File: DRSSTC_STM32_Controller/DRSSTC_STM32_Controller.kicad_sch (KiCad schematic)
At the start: 4 parts, among them J2 Conn_01x04

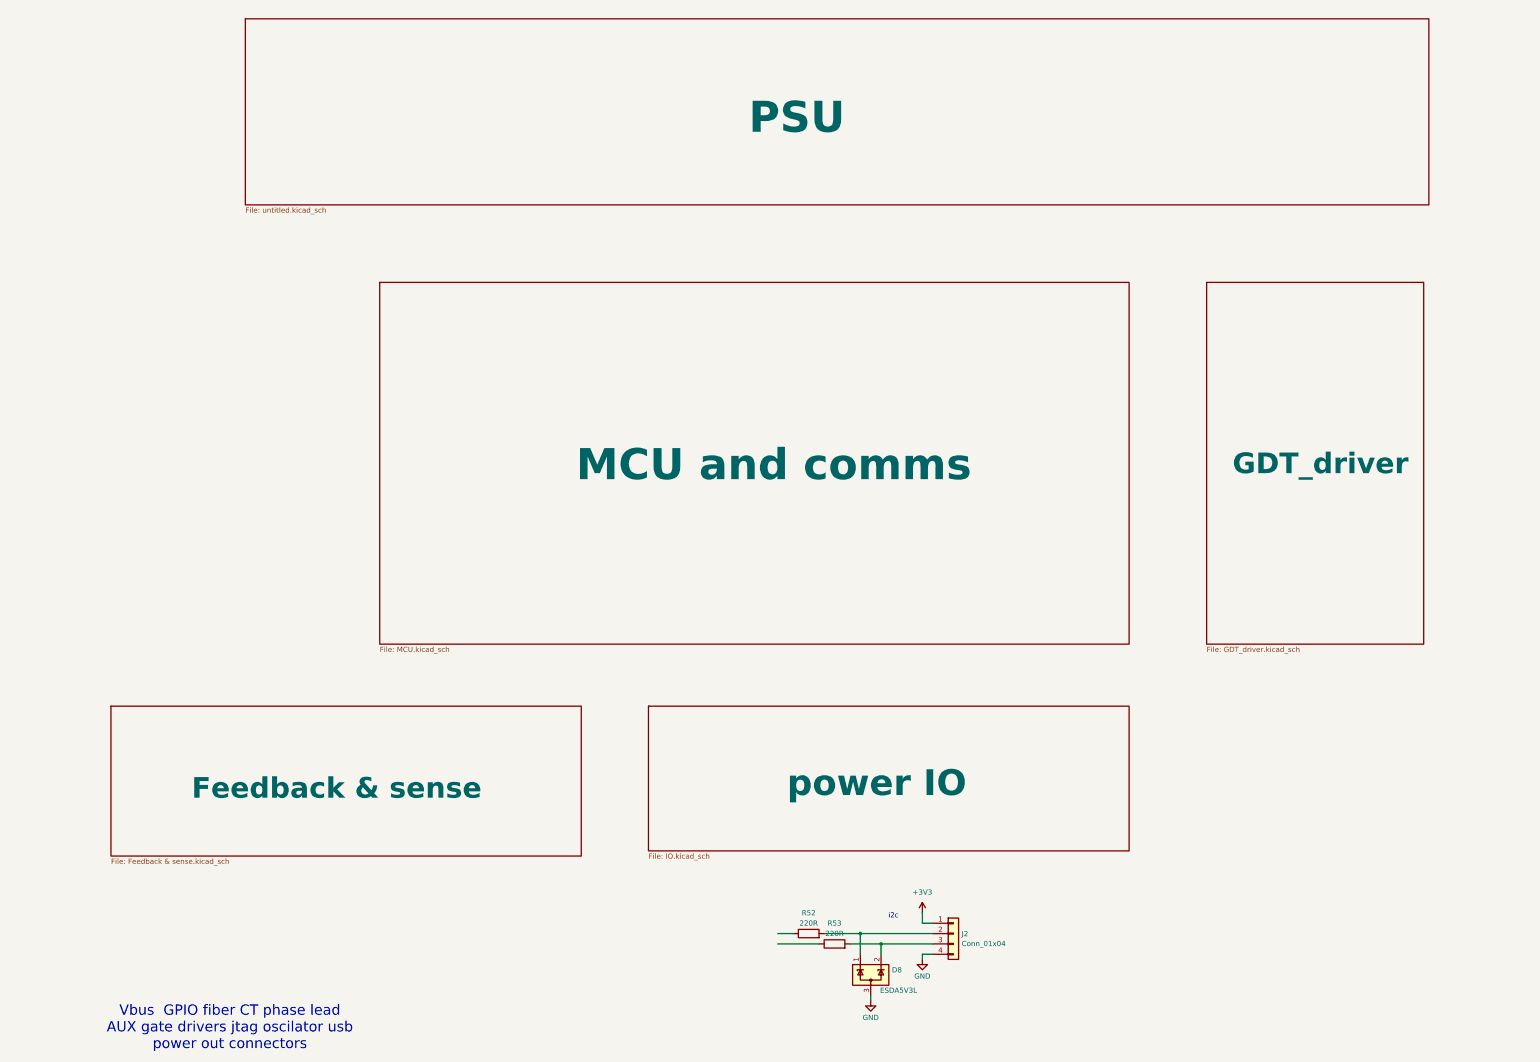
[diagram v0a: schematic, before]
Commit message: update the feedback stage simulation & controller schematic
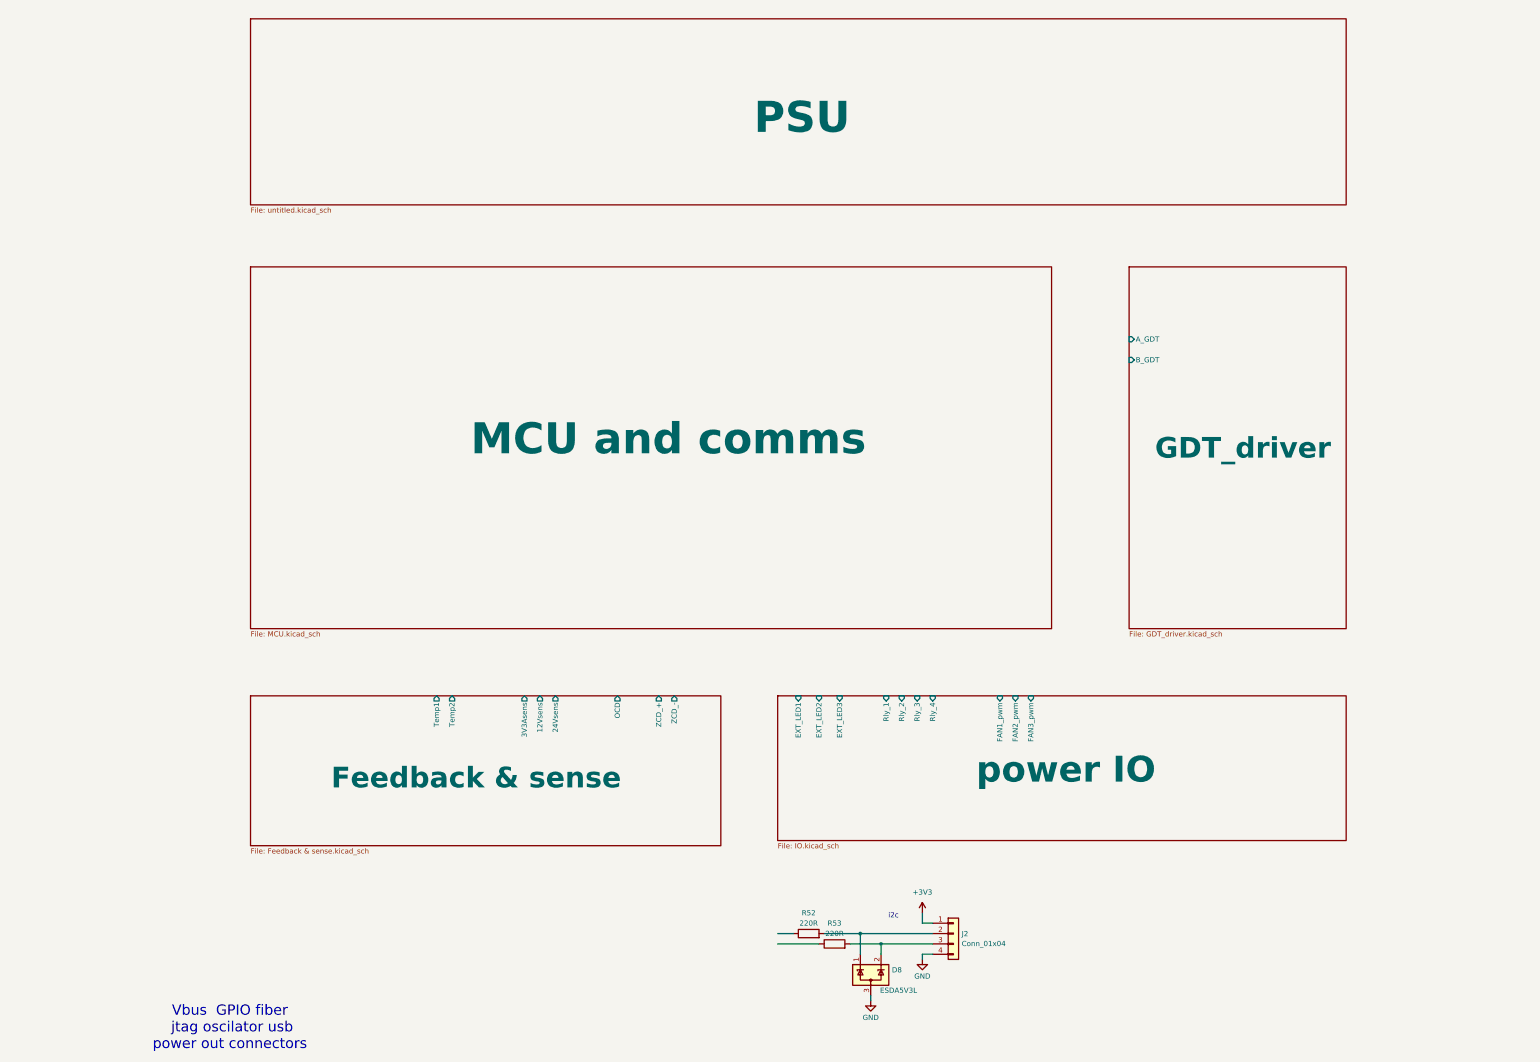
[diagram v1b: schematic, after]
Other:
- sheet Feedback & sense ports: added 12Vsens, 24Vsens, 3V3Asens, OCD, Temp1, Temp2, ZCD_+, ZCD_-; removed none
- sheet GDT_driver ports: added A_GDT, B_GDT; removed none
- sheet power IO ports: added EXT_LED1, EXT_LED2, EXT_LED3, FAN1_pwm, FAN2_pwm, FAN3_pwm, Rly_1, Rly_2, Rly_3, Rly_4; removed none
- note added: "Vbus GPIO fiber jtag oscilator usb power out connectors"
- note removed: "Vbus GPIO fiber CT phase lead AUX gate drivers jtag oscilator usb power out connectors"
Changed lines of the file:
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@@
 	(generator_version "10.0")
 	(paper "A3")
-	(text "Vbus  GPIO fiber CT phase lead\nAUX gate drivers jtag oscilator usb\npower out connectors"
+	(text "Vbus  GPIO fiber \n jtag oscilator usb\npower out connectors"
 		(exclude_from_sim no)
 		(at 72.39 270.764 0)
@@
 	)
 	(sheet
-		(at 312.42 87.63)
+		(at 293.37 83.82)
 		(size 53.34 88.9)
 		(exclude_from_sim no)
@@
 		)
 		(property "Sheetname" "GDT_driver"
-			(at 318.77 135.128 0)
+			(at 299.72 131.318 0)
 			(show_name no)
 			(do_not_autoplace no)
@@
 		)
 		(property "Sheetfile" "GDT_driver.kicad_sch"
-			(at 312.42 177.1146 0)
+			(at 293.37 173.3046 0)
 			(show_name no)
 			(do_not_autoplace no)
@@
 				)
 				(justify left top)
+			)
+		)
+		(pin "A_GDT" input
+			(at 293.37 101.6 180)
+			(effects
+				(font
+					(size 1.27 1.27)
+				)
+				(justify left)
+			)
+		)
+		(pin "B_GDT" input
+			(at 293.37 106.68 180)
+			(effects
+				(font
+					(size 1.27 1.27)
+				)
+				(justify left)
 			)
 		)
@@
 	)
 	(sheet
-		(at 109.22 87.63)
-		(size 184.15 88.9)
+		(at 77.47 83.82)
+		(size 196.85 88.9)
 		(exclude_from_sim no)
 		(in_bom yes)
@@
 		)
 		(property "Sheetname" "MCU and comms"
-			(at 157.48 136.906 0)
+			(at 131.572 130.556 0)
 			(show_name no)
 			(do_not_autoplace no)
@@
 		)
 		(property "Sheetfile" "MCU.kicad_sch"
-			(at 109.22 177.1146 0)
+			(at 77.47 173.3046 0)
 			(show_name no)
 			(do_not_autoplace no)
@@
 	)
 	(sheet
-		(at 76.2 22.86)
-		(size 290.83 45.72)
+		(at 77.47 22.86)
+		(size 269.24 45.72)
 		(exclude_from_sim no)
 		(in_bom yes)
@@
 		)
 		(property "Sheetname" "PSU"
-			(at 199.898 51.562 0)
+			(at 201.168 51.562 0)
 			(show_name no)
 			(do_not_autoplace no)
@@
 		)
 		(property "Sheetfile" "untitled.kicad_sch"
-			(at 76.2 69.1646 0)
+			(at 77.47 69.1646 0)
 			(show_name no)
 			(do_not_autoplace no)
@@
 	)
 	(sheet
-		(at 43.18 191.77)
+		(at 77.47 189.23)
 		(size 115.57 36.83)
 		(exclude_from_sim no)
@@
 		)
 		(property "Sheetname" "Feedback & sense"
-			(at 62.992 214.884 0)
+			(at 97.282 212.344 0)
 			(show_name no)
 			(do_not_autoplace no)
@@
 		)
 		(property "Sheetfile" "Feedback & sense.kicad_sch"
-			(at 43.18 229.1846 0)
+			(at 77.47 226.6446 0)
 			(show_name no)
 			(do_not_autoplace no)
@@
 				)
 				(justify left top)
+			)
+		)
+		(pin "3V3Asens" output
+			(at 144.78 189.23 90)
+			(effects
+				(font
+					(size 1.27 1.27)
+				)
+				(justify right)
+			)
+		)
+		(pin "12Vsens" output
+			(at 148.59 189.23 90)
+			(effects
+				(font
+					(size 1.27 1.27)
+				)
+				(justify right)
+			)
+		)
+		(pin "24Vsens" output
+			(at 152.4 189.23 90)
+			(effects
+				(font
+					(size 1.27 1.27)
+				)
+				(justify right)
+			)
+		)
+		(pin "OCD" output
+			(at 167.64 189.23 90)
+			(effects
+				(font
+					(size 1.27 1.27)
+				)
+				(justify right)
+			)
+		)
+		(pin "Temp1" output
+			(at 123.19 189.23 90)
+			(effects
+				(font
+					(size 1.27 1.27)
+				)
+				(justify right)
+			)
+		)
+		(pin "Temp2" output
+			(at 127 189.23 90)
+			(effects
+				(font
+					(size 1.27 1.27)
+				)
+				(justify right)
+			)
+		)
+		(pin "ZCD_+" output
+			(at 177.8 189.23 90)
+			(effects
+				(font
+					(size 1.27 1.27)
+				)
+				(justify right)
+			)
+		)
+		(pin "ZCD_-" output
+			(at 181.61 189.23 90)
+			(effects
+				(font
+					(size 1.27 1.27)
+				)
+				(justify right)
 			)
 		)
@@
 	)
 	(sheet
-		(at 175.26 191.77)
-		(size 118.11 35.56)
+		(at 207.01 189.23)
+		(size 139.7 35.56)
 		(exclude_from_sim no)
 		(in_bom yes)
@@
 		)
 		(property "Sheetname" "power IO"
-			(at 209.296 214.376 0)
+			(at 255.778 211.074 0)
 			(show_name no)
 			(do_not_autoplace no)
@@
 		)
 		(property "Sheetfile" "IO.kicad_sch"
-			(at 175.26 227.9146 0)
+			(at 207.01 225.3746 0)
 			(show_name no)
 			(do_not_autoplace no)
@@
 			)
 		)
+		(pin "EXT_LED1" input
+			(at 212.09 189.23 90)
+			(effects
+				(font
+					(size 1.27 1.27)
+				)
+				(justify right)
+			)
+		)
+		(pin "EXT_LED2" input
+			(at 217.17 189.23 90)
+			(effects
+				(font
+					(size 1.27 1.27)
+				)
+				(justify right)
+			)
+		)
+		(pin "EXT_LED3" input
+			(at 222.25 189.23 90)
+			(effects
+				(font
+					(size 1.27 1.27)
+				)
+				(justify right)
+			)
+		)
+		(pin "FAN1_pwm" input
+			(at 261.62 189.23 90)
+			(effects
+				(font
+					(size 1.27 1.27)
+				)
+				(justify right)
+			)
+		)
+		(pin "FAN2_pwm" input
+			(at 265.43 189.23 90)
+			(effects
+				(font
+					(size 1.27 1.27)
+				)
+				(justify right)
+			)
+		)
+		(pin "FAN3_pwm" input
+			(at 269.24 189.23 90)
+			(effects
+				(font
+					(size 1.27 1.27)
+				)
+				(justify right)
+			)
+		)
+		(pin "Rly_1" input
+			(at 233.68 189.23 90)
+			(effects
+				(font
+					(size 1.27 1.27)
+				)
+				(justify right)
+			)
+		)
+		(pin "Rly_2" input
+			(at 237.49 189.23 90)
+			(effects
+				(font
+					(size 1.27 1.27)
+				)
+				(justify right)
+			)
+		)
+		(pin "Rly_3" input
+			(at 241.3 189.23 90)
+			(effects
+				(font
+					(size 1.27 1.27)
+				)
+				(justify right)
+			)
+		)
+		(pin "Rly_4" input
+			(at 245.11 189.23 90)
+			(effects
+				(font
+					(size 1.27 1.27)
+				)
+				(justify right)
+			)
+		)

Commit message: update conroller schematics
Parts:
- removed D8: ESDA5V3L, Package_TO_SOT_SMD:SOT-23-3, symbol Power_Protection:ESDA5V3L
- removed J2: Conn_01x04, symbol Connector_Generic:Conn_01x04
- removed R52, R53: 220R, Resistor_SMD:R_0805_2012Metric, symbol Device:R
- added C48: 10n, Capacitor_SMD:C_0805_2012Metric, symbol Device:C
- added C49: 10u, Capacitor_SMD:C_0805_2012Metric, symbol Device:C
- added D42, D44: D_Schottky, symbol Device:D_Schottky
- added J1, J10, J11, J16, J7: Conn_01x04, symbol Connector_Generic:Conn_01x04
- added J13: USB_C_Receptacle_USB2.0_14P, symbol Connector:USB_C_Receptacle_USB2.0_14P
- added J28, J29, J30, J31, J32, J33, J34, J35, J36, J37, J38, J39, J4, J40, J41, J42: Screw_Terminal_01x02, TerminalBlock_Altech:Altech_AK100_1x02_P5.00mm, symbol Connector:Screw_Terminal_01x02
- added J5, J6: Conn_01x01, symbol Connector_Generic:Conn_01x01
- added JP4: SolderJumper_2_Bridged, symbol Jumper:SolderJumper_2_Bridged
- added R76: 1M, Resistor_SMD:R_0805_2012Metric, symbol Device:R
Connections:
- net +3V3: now also D44.1 (K)
- net GND: now also C48.2, C49.2, J1.1 (Pin_1), J10.1 (Pin_1), J11.1 (Pin_1), J13.A1 (GND), J13.A12 (GND), J13.B1 (GND), J13.B12 (GND), J16.1 (Pin_1), J28.2 (Pin_2), J29.2 (Pin_2), J30.2 (Pin_2), J31.2 (Pin_2), J4.1 (Pin_1), J7.1 (Pin_1), JP4.1 (A), R76.1
- new net: D42.2 (A), J13.A4 (VBUS), J13.A9 (VBUS), J13.B4 (VBUS), J13.B9 (VBUS)
- new net: C48.1, J13.SH (SHIELD), JP4.2 (B), R76.2
- new net: D44.2 (A), J16.4 (Pin_4)
- new net +12V: J1.2 (Pin_2), J10.2 (Pin_2), J11.2 (Pin_2), J34.1 (Pin_1), J35.1 (Pin_1), J36.1 (Pin_1), J37.1 (Pin_1), J38.1 (Pin_1), J39.1 (Pin_1), J40.1 (Pin_1), J41.1 (Pin_1), J7.2 (Pin_2)
- new net +24V: C49.1, D42.1 (K)
- new net Feedback & sensing/CT+: J42.2 (Pin_2)
- new net Feedback & sensing/CT-: J42.1 (Pin_1)
- new net Feedback & sensing/Vbus+: J5.1 (Pin_1)
- new net Feedback & sensing/Vbus-: J6.1 (Pin_1)
- new net GDT_driver/GDT1+: J32.1 (Pin_1)
- new net GDT_driver/GDT1-: J32.2 (Pin_2)
- new net GDT_driver/GDT2+: J33.1 (Pin_1)
- new net GDT_driver/GDT2-: J33.2 (Pin_2)
- new net MCU and comms/SYS_JTCK-SWCLK: J16.2 (Pin_2)
- new net MCU and comms/SYS_JTMS-SWDIO: J16.3 (Pin_3)
- new net MCU and comms/USB+: J13.A6 (D+), J13.B6 (D+)
- new net MCU and comms/USB-: J13.A7 (D-), J13.B7 (D-)
- new net MCU and comms/USB_CC1: J13.A5 (CC1)
- new net MCU and comms/USB_CC2: J13.B5 (CC2)
- new net PSU/12V: J29.1 (Pin_1)
- new net PSU/24V: J28.1 (Pin_1)
- new net PSU/24Vin: J4.2 (Pin_2)
- new net PSU/3V3: J31.1 (Pin_1)
- new net PSU/3V3A: J30.1 (Pin_1)
- new net power IO/FAN1cntrl: J1.4 (Pin_4)
- new net power IO/FAN2cntrl: J7.4 (Pin_4)
- new net power IO/FAN3cntrl: J10.4 (Pin_4)
- new net power IO/FAN4cntrl: J11.4 (Pin_4)
- new net power IO/LED1: J38.2 (Pin_2)
- new net power IO/LED2: J39.2 (Pin_2)
- new net power IO/LED3: J40.2 (Pin_2)
- new net power IO/LED4: J41.2 (Pin_2)
- new net power IO/Relay1: J37.2 (Pin_2)
- new net power IO/Relay2: J36.2 (Pin_2)
- new net power IO/Relay3: J35.2 (Pin_2)
- new net power IO/Relay4: J34.2 (Pin_2)
- no-connect marks 0 -> 4
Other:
- sheet Feedback & sense renamed Feedback & sensing
- sheet Feedback & sensing ports: added 3V3sens, CT+, CT-, OPAMP+, OPAMP-, OPAMP_out, Temp3, Temp4, Vbus+, Vbus-; removed none
- sheet GDT_driver ports: added G1+, G1-, G2+, G2-, GDT1+, GDT1-, GDT2+, GDT2-; removed A_GDT, B_GDT
- sheet MCU and comms ports: added 12V_EN, 12Vsense, 24Vsense, 3V3Asense, 3V3sense, EXT_LED1, EXT_LED2, EXT_LED3, EXT_LED4, FAN1_pwm, FAN2_pwm, FAN3_pwm, FAN4_pwm, G1+, G1-, G2+, G2-, OCD, OPAMP+, OPAMP-, OPAMP_out, Rly_1, Rly_2, Rly_3, Rly_4, SYS_JTCK-SWCLK, SYS_JTMS-SWDIO, Temp1, Temp2, Temp3, Temp4, USB+, USB-, USB_CC1, USB_CC2, ZCD_+, ZCD_-; removed none
- sheet PSU ports: added 12V, 12V_EN, 24V, 24Vin, 3V3, 3V3A; removed none
- sheet power IO ports: added EXT_LED4, FAN1cntrl, FAN2cntrl, FAN3cntrl, FAN4_pwm, FAN4cntrl, LED1, LED2, LED3, LED4, Relay1, Relay2, Relay3, Relay4; removed none
- note added: "24V 2A (more for fans and EXT_LEDs)"
- note added: "AUX Supply"
- note added: "External rsistors!"
- note added: "FANs"
- note added: "GDT1"
- note added: "GDT2"
- note added: "LEDs"
- note added: "Relays"
- note added: "solder the CT directly"
- note added: "solder the GDT directly"
- note removed: "Vbus GPIO fiber jtag oscilator usb power out connectors"
- note removed: "i2c"

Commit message: assign footprints
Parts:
- removed J34, J35, J36, J37, J38, J39, J40, J41: Screw_Terminal_01x02, TerminalBlock_Altech:Altech_AK100_1x02_P5.00mm, symbol Connector:Screw_Terminal_01x02
- removed J5, J6: Conn_01x01, symbol Connector_Generic:Conn_01x01
- added J12, J14, J17: Conn_01x10, Library:terminal 10pin, symbol Connector_Generic:Conn_01x10
- added J5, J6: Conn_Coaxial, Connector_Coaxial:BNC_TEConnectivity_1478204_Vertical, symbol Connector:Conn_Coaxial
- C48: footprint Capacitor_SMD:C_0805_2012Metric -> Capacitor_SMD:C_0603_1608Metric
- D42, D44: footprint (none) -> Diode_SMD:D_SOD-128
- J1, J10, J11, J7: footprint (none) -> Library:4PIN SMD 2.54
- J13: footprint (none) -> Connector_USB:USB_C_Receptacle_HCTL_HC-TYPE-C-16P-01A
- J16: footprint (none) -> Connector_PinHeader_2.54mm:PinHeader_1x04_P2.54mm_Vertical
- J28, J29, J30, J31, J32, J33, J42: footprint TerminalBlock_Altech:Altech_AK100_1x02_P5.00mm -> TerminalBlock_MetzConnect:TerminalBlock_MetzConnect_Type094_RT03502HBLU_1x02_P5.00mm_Horizontal
- J4: footprint TerminalBlock_Altech:Altech_AK100_1x02_P5.00mm -> TerminalBlock_MetzConnect:TerminalBlock_MetzConnect_Type055_RT01502HDWU_1x02_P5.00mm_Horizontal
- JP4: footprint (none) -> Jumper:SolderJumper-2_P1.3mm_Bridged2Bar_RoundedPad1.0x1.5mm
- R76: footprint Resistor_SMD:R_0805_2012Metric -> Resistor_SMD:R_0603_1608Metric
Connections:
- net +12V: now also J12.3 (Pin_3), J12.5 (Pin_5), J12.7 (Pin_7), J12.9 (Pin_9), J17.3 (Pin_3), J17.5 (Pin_5), J17.7 (Pin_7), J17.9 (Pin_9)
- net Feedback & sensing/Vbus+: now also J5.1 (In)
- net Feedback & sensing/Vbus-: now also J6.1 (In)
- net GND: now also J12.2 (Pin_2), J14.3 (Pin_3), J14.5 (Pin_5), J14.7 (Pin_7), J14.9 (Pin_9), J17.2 (Pin_2), J5.2 (Ext), J6.2 (Ext)
- net power IO/LED1: now also J12.10 (Pin_10)
- net power IO/LED2: now also J12.8 (Pin_8)
- net power IO/LED3: now also J12.6 (Pin_6)
- net power IO/LED4: now also J12.4 (Pin_4)
- net power IO/Relay1: now also J17.4 (Pin_4)
- net power IO/Relay2: now also J17.6 (Pin_6)
- net power IO/Relay3: now also J17.8 (Pin_8)
- net power IO/Relay4: now also J17.10 (Pin_10)
- new net Feedback & sensing/NTC1: J14.10 (Pin_10)
- new net Feedback & sensing/NTC2: J14.8 (Pin_8)
- new net Feedback & sensing/NTC3: J14.6 (Pin_6)
- new net Feedback & sensing/NTC4: J14.4 (Pin_4)
- new net MCU and comms/GPIO_1: J17.1 (Pin_1)
- new net MCU and comms/GPIO_2: J12.1 (Pin_1)
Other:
- sheet Feedback & sensing ports: added NTC1, NTC2, NTC3, NTC4; removed none
- sheet MCU and comms ports: added GPIO_1, GPIO_2; removed none
- moved on the sheet: C48, C49, D42, D44, J13, J16, J42, JP4, R76
